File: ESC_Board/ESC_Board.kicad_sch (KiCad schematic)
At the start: 65 parts, among them J1 63824-1, J2 63824-1, J3 63824-1, Q1 AO3400A, Q3 SIR182DP, Q4 SIR182DP, Q5 SIR182DP, Q6 SIR182Dp, Q7 SIR182DP, Q8 SIR182DP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

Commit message: ESC Board: Major overhauls to schematic, preliminary layout
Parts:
- removed C52: 1uF, PCM_JLCPCB:C_0603, symbol PCM_JLCPCB-Capacitors:0603,1uF
- removed R10, R12: 10kΩ, PCM_JLCPCB:R_0402, symbol PCM_JLCPCB-Resistors:0402,10kΩ
- removed R8, R9: 22Ω, PCM_JLCPCB:R_0402, symbol PCM_JLCPCB-Resistors:0402,22Ω
- removed TP1, TP2: TestPoint_2Pole, symbol Connector:TestPoint_2Pole
- added C52, C55: 22pF, PCM_JLCPCB:C_0402, symbol PCM_JLCPCB-Capacitors:0402,22pF
- added C8: 100uF, Capacitor_SMD:CP_Elec_8x10, symbol Device:C_Polarized_Small
- added J4: Conn_01x02_Pin, Connector_AMASS:AMASS_XT60-F_1x02_P7.20mm_Vertical, symbol Connector:Conn_01x02_Pin
- added J5: Conn_01x04_Pin, Connector_PinHeader_1.00mm:PinHeader_1x04_P1.00mm_Vertical, symbol Connector:Conn_01x04_Pin
- added R1, R5: 100Ω, PCM_JLCPCB:R_0402, symbol PCM_JLCPCB-Resistors:0402,100Ω
- added SW1, SW2: SW_SPST, easy:SW-SMD_2P-L3.5-W6.2-P2.54-LS9.8, symbol Switch:SW_SPST
- added Y1: Crystal_Small, easy:OSC-SMD_2P-L3.2-W2.5, symbol Device:Crystal_Small
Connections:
- net -LiPo is gone; now on net GND: D8.2
- net AGND is gone; now on net GND: U4.6 (AGND)
- net +17V: now also C8.1, J4.1 (Pin_1)
- net +3.3V: now also R11.1, J5.3 (Pin_3)
- net GND: now also C52.2, C55.2, C8.2, J4.2 (Pin_2), J5.4 (Pin_4), SW1.2 (B); no longer R11.1
- net SWCLK: now also J5.1 (Pin_1), R5.2
- net SWDIO: now also J5.2 (Pin_2), R1.2
- net at Q1.1 (G): now also U2.25 (PA15); no longer U2.32 (PB8)
- net at R11.2: now also SW2.2 (B)
- net at U2.31 (BOOT0): now also SW2.1 (A)
- net at U2.23 (PA13): now also R1.1
- net at U2.24 (PA14): now also R5.1
- net at U2.2 (PF0): now also C55.1, Y1.1
- net at U2.3 (PF1): now also C52.1, Y1.2
- net SWDR: no longer names the net of U2.4 (NRST)
- net SWDR: now also SW1.1 (A)
- no-connect marks 13 -> 12
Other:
- moved on the sheet: D1, Q1, R11, R3

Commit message: Finalized Layout for ESC Board
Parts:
- added J6: Conn_01x02_Pin, JST_EH_B2B-EH-A_1x02_P2.50mm_Vertical, symbol Connector:Conn_01x02_Pin
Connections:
- net +3.3V: now also J6.1 (Pin_1)
- net GND: now also J6.2 (Pin_2)
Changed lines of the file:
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@@
 	)
 	(symbol
+		(lib_id "power:GND")
+		(at 232.41 170.18 90)
+		(unit 1)
+		(exclude_from_sim no)
+		(in_bom yes)
+		(on_board yes)
+		(dnp no)
+		(fields_autoplaced yes)
+		(property "Reference" "#PWR0118"
+			(at 238.76 170.18 0)
+			(effects
+				(font
+					(size 1.27 1.27)
+				)
+				(hide yes)
+			)
+		)
+		(property "Value" "GND"
+			(at 236.22 170.1799 90)
+			(effects
+				(font
+					(size 1.27 1.27)
+				)
+				(justify right)
+			)
+		)
+		(property "Footprint" ""
+			(at 232.41 170.18 0)
+			(effects
+				(font
+					(size 1.27 1.27)
+				)
+				(hide yes)
+			)
+		)
+		(property "Datasheet" ""
+			(at 232.41 170.18 0)
+			(effects
+				(font
+					(size 1.27 1.27)
+				)
+				(hide yes)
+			)
+		)
+		(property "Description" "Power symbol creates a global label with name \"GND\" , ground"
+			(at 232.41 170.18 0)
+			(effects
+				(font
+					(size 1.27 1.27)
+				)
+				(hide yes)
+			)
+		)
+		(pin "1"
+		)
+		(instances
+			(project ""
+				(path "/c7f275f7-0597-4a7d-8593-149a5f6bff0e"
+					(reference "#PWR0118")
+					(unit 1)
+				)
+			)
+		)
+	)
+	(symbol
 		(lib_id "power:+3.3V")
 		(at 212.09 173.99 270)
@@
 	)
 	(symbol
+		(lib_id "power:+3.3V")
+		(at 232.41 167.64 270)
+		(unit 1)
+		(exclude_from_sim no)
+		(in_bom yes)
+		(on_board yes)
+		(dnp no)
+		(fields_autoplaced yes)
+		(property "Reference" "#PWR0107"
+			(at 228.6 167.64 0)
+			(effects
+				(font
+					(size 1.27 1.27)
+				)
+				(hide yes)
+			)
+		)
+		(property "Value" "+3.3V"
+			(at 236.22 167.6399 90)
+			(effects
+				(font
+					(size 1.27 1.27)
+				)
+				(justify left)
+			)
+		)
+		(property "Footprint" ""
+			(at 232.41 167.64 0)
+			(effects
+				(font
+					(size 1.27 1.27)
+				)
+				(hide yes)
+			)
+		)
+		(property "Datasheet" ""
+			(at 232.41 167.64 0)
+			(effects
+				(font
+					(size 1.27 1.27)
+				)
+				(hide yes)
+			)
+		)
+		(property "Description" "Power symbol creates a global label with name \"+3.3V\""
+			(at 232.41 167.64 0)
+			(effects
+				(font
+					(size 1.27 1.27)
+				)
+				(hide yes)
+			)
+		)
+		(pin "1"
+		)
+		(instances
+			(project ""
+				(path "/c7f275f7-0597-4a7d-8593-149a5f6bff0e"
+					(reference "#PWR0107")
+					(unit 1)
+				)
+			)
+		)
+	)
+	(symbol
 		(lib_id "PCM_JLCPCB-Resistors:0402,22Ω")
 		(at 227.33 24.13 90)
@@
 					(unit 1)
 				)
+			)
+		)
+	)
+	(symbol
+		(lib_id "Connector:Conn_01x02_Pin")
+		(at 227.33 167.64 0)
+		(unit 1)
+		(exclude_from_sim no)
+		(in_bom yes)
+		(on_board yes)
+		(dnp no)
+		(fields_autoplaced yes)
+		(property "Reference" "J6"
+			(at 227.965 162.56 0)
+			(effects
+				(font
+					(size 1.27 1.27)
+				)
+			)
+		)
+		(property "Value" "Conn_01x02_Pin"
+			(at 227.965 165.1 0)
+			(effects
+				(font
+					(size 1.27 1.27)
+				)
+				(hide yes)
+			)
+		)
+		(property "Footprint" "JST_EH_B2B-EH-A_1x02_P2.50mm_Vertical"
+			(at 227.33 167.64 0)
+			(effects
+				(font
+					(size 1.27 1.27)
+				)
+				(hide yes)
+			)
+		)
+		(property "Datasheet" "~"
+			(at 227.33 167.64 0)
+			(effects
+				(font
+					(size 1.27 1.27)
+				)
+				(hide yes)
+			)
+		)
+		(property "Description" "Generic connector, single row, 01x02, script generated"
+			(at 227.33 167.64 0)
+			(effects
+				(font
+					(size 1.27 1.27)
+				)
+				(hide yes)
+			)
+		)
+		(pin "1"
+		)
+		(pin "2"
+		)
+		(instances
+			(project ""
+				(path "/c7f275f7-0597-4a7d-8593-149a5f6bff0e"
+					(reference "J6")
+					(unit 1)
+				)

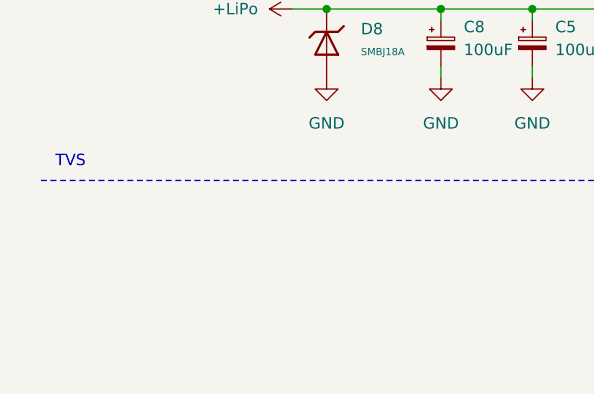
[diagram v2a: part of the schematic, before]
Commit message: Optimized Signal Integrity, added stichting vias, and stiching capacitors between PWR and GND layers
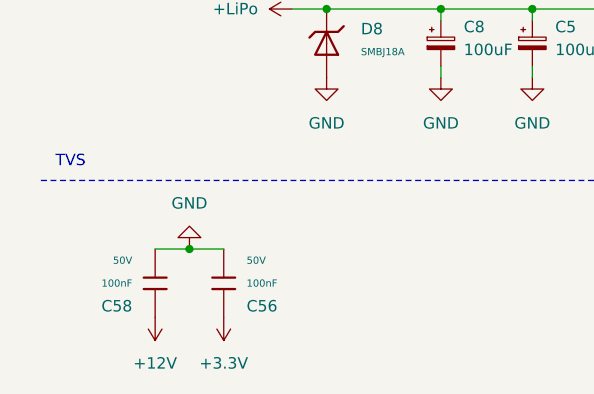
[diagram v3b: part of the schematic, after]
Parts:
- added C56, C58: 100nF, PCM_JLCPCB:C_0402, symbol PCM_JLCPCB-Capacitors:0402,100nF,(2)
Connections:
- net +12V: now also C58.1
- net +3.3V: now also C56.1
- net GND: now also C56.2, C58.2
